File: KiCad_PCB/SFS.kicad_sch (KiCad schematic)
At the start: 28 parts, among them J4 Screw_Terminal_01x02, J6 Screw_Terminal_01x04, Q1 IRF9540N, Q2 IRLB4132, Q3 2N7000, SW1 SW_Push, SW2 SW_Push, U4 DS3231, U6 L7806

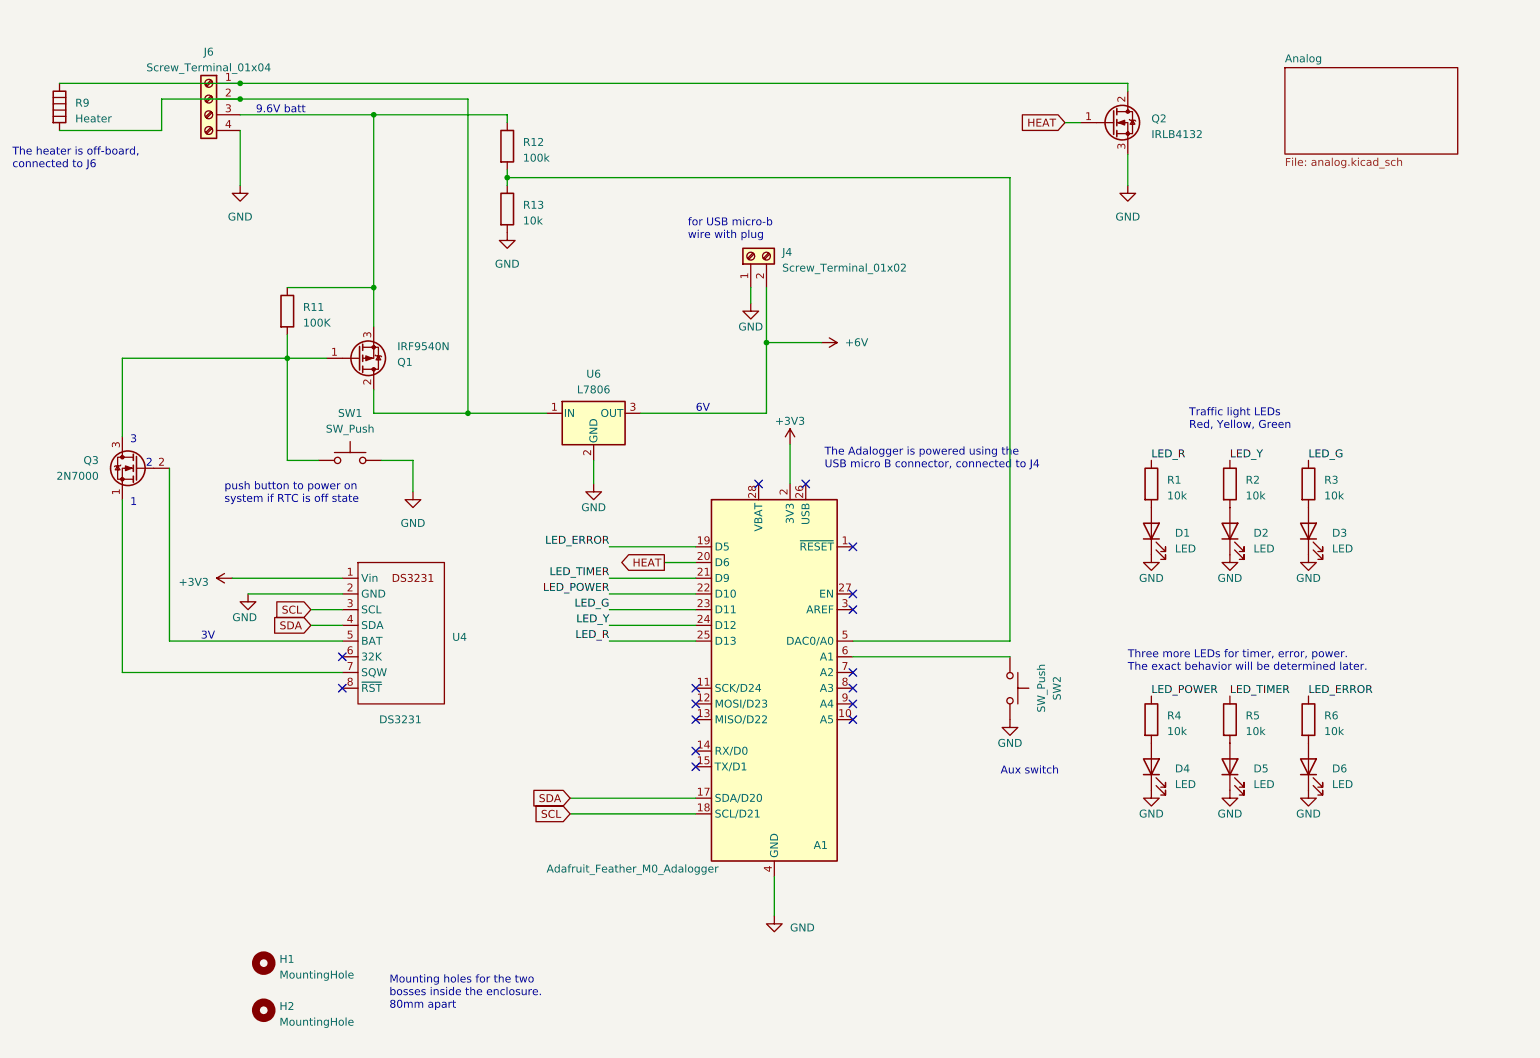
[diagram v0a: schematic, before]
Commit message: updated kicad
Updated to v2.1 from evonne's github
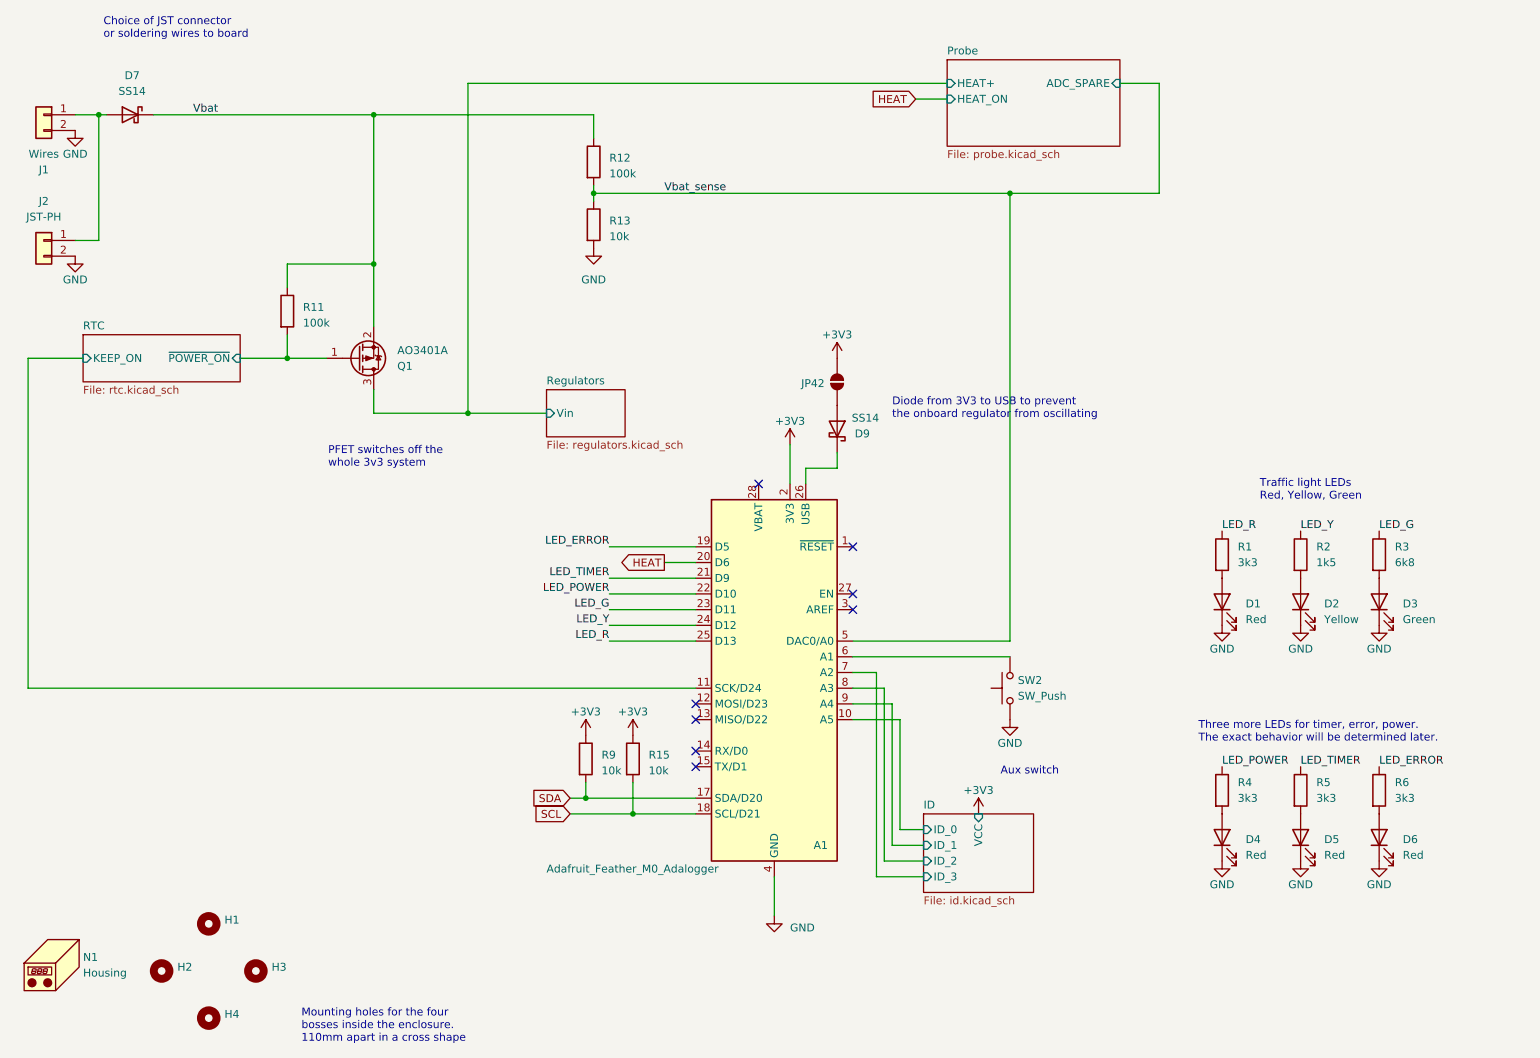
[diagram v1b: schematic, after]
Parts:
- removed J4: Screw_Terminal_01x02, SapFlow_Footprints:Wurth_Screwless45_3.81mm_2, symbol Connector:Screw_Terminal_01x02
- removed J6: Screw_Terminal_01x04, SapFlow_Footprints:Wurth_Screwless45_3.81mm_4, symbol Connector:Screw_Terminal_01x04
- removed Q1: IRF9540N, Package_TO_SOT_THT:TO-262-3_Vertical, symbol Transistor_FET:IRF9540N
- removed Q2: IRLB4132, Package_TO_SOT_THT:TO-262-3_Vertical, symbol Device:Q_NMOS_GDS
- removed Q3: 2N7000, Package_TO_SOT_THT:TO-92_Inline, symbol Transistor_FET:2N7000
- removed R9: Heater, symbol Device:Heater
- removed SW1: SW_Push, Button_Switch_THT:SW_PUSH_6mm_H4.3mm, symbol Switch:SW_Push
- removed U4: DS3231, SapFlow_Footprints:DS3231_Breakout_RightAngle, symbol New_Library:DS3231_Breakout
- removed U6: L7806, Package_TO_SOT_THT:TO-220-3_Vertical, symbol Regulator_Linear:L7806
- added D7, D9: SS14, Diode_SMD:D_SMA, symbol Diode:SS14
- added H3, H4: MountingHole, MountingHole:MountingHole_4.3mm_M4, symbol Mechanical:MountingHole
- added J1: Wires, Connector_Wire:SolderWire-0.25sqmm_1x02_P4.2mm_D0.65mm_OD1.7mm_Relief, symbol Connector_Generic:Conn_01x02
- added J2: JST-PH, Connector_JST:JST_PH_B2B-PH-K_1x02_P2.00mm_Vertical, symbol Connector_Generic:Conn_01x02
- added JP42: SolderJumper_2_Open, Jumper:SolderJumper-2_P1.3mm_Open_Pad1.0x1.5mm, symbol Jumper:SolderJumper_2_Open
- added N1: Housing, SapFlow_Footprints:Enclosure_WH-10, symbol Mechanical:Housing
- added Q1: AO3401A, Package_TO_SOT_SMD:SOT-23, symbol Transistor_FET:AO3401A
- added R15, R9: 10k, Resistor_SMD:R_0805_2012Metric_Pad1.20x1.40mm_HandSolder, symbol Device:R
- D1, D4, D5, D6: value LED -> Red; footprint LED_THT:LED_D3.0mm -> LED_SMD:LED_0603_1608Metric_Pad1.05x0.95mm_HandSolder; LCSC (none) -> C2286
- D2: value LED -> Yellow; footprint LED_THT:LED_D3.0mm -> LED_SMD:LED_0805_2012Metric_Pad1.15x1.40mm_HandSolder; LCSC (none) -> C2296
- D3: value LED -> Green; footprint LED_THT:LED_D3.0mm -> LED_SMD:LED_0805_2012Metric_Pad1.15x1.40mm_HandSolder; LCSC (none) -> C2297
- R1, R4, R5, R6: value 10k -> 3k3; footprint Resistor_THT:R_Axial_DIN0204_L3.6mm_D1.6mm_P7.62mm_Horizontal -> Resistor_SMD:R_0805_2012Metric_Pad1.20x1.40mm_HandSolder; LCSC (none) -> C26010
- R11: value 100K -> 100k; footprint Resistor_THT:R_Axial_DIN0204_L3.6mm_D1.6mm_P2.54mm_Vertical -> Resistor_SMD:R_0805_2012Metric_Pad1.20x1.40mm_HandSolder; LCSC (none) -> C149504
- R12: footprint Resistor_THT:R_Axial_DIN0204_L3.6mm_D1.6mm_P2.54mm_Vertical -> Resistor_SMD:R_0805_2012Metric_Pad1.20x1.40mm_HandSolder; LCSC (none) -> C149504
- R13: footprint Resistor_THT:R_Axial_DIN0204_L3.6mm_D1.6mm_P2.54mm_Vertical -> Resistor_SMD:R_0805_2012Metric_Pad1.20x1.40mm_HandSolder; LCSC (none) -> C17414
- R2: value 10k -> 1k5; footprint Resistor_THT:R_Axial_DIN0204_L3.6mm_D1.6mm_P7.62mm_Horizontal -> Resistor_SMD:R_0805_2012Metric_Pad1.20x1.40mm_HandSolder; LCSC (none) -> C4310
- R3: value 10k -> 6k8; footprint Resistor_THT:R_Axial_DIN0204_L3.6mm_D1.6mm_P7.62mm_Horizontal -> Resistor_SMD:R_0805_2012Metric_Pad1.20x1.40mm_HandSolder; LCSC (none) -> C17772
- SW2: footprint Button_Switch_THT:SW_PUSH_6mm_H4.3mm -> AAA_Library:SW_Push_1P1T_NO_6x6mm_H9.5mm_C2837532; LCSC (none) -> C2837532
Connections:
- net +3V3: now also JP42.2 (B), R15.1, R9.1
- net GND: now also J1.2 (Pin_2), J2.2 (Pin_2)
- net SCL: now also R15.2
- net SDA: now also R9.2
- net RTC/~{POWER_ON}: now reaches R11.2
- net RTC/~{POWER_ON}: now also Q1.1 (G)
- net Vbat_sense: now reaches A1.5 (DAC0/A0), R12.2, R13.1
- net Vbat: now reaches R11.1, R12.1
- net Vbat: now also D7.1 (K), Q1.2 (S)
- net ID/ID_0: now reaches A1.10 (A5)
- net RTC/KEEP_ON: now reaches A1.11 (SCK/D24)
- net at A1.26 (USB): now also D9.1 (K)
- net ID/ID_3: now reaches A1.7 (A2)
- net ID/ID_2: now reaches A1.8 (A3)
- net ID/ID_1: now reaches A1.9 (A4)
- new net: D7.2 (A), J1.1 (Pin_1), J2.1 (Pin_1)
- new net: D9.2 (A), JP42.1 (A)
- new net Probe/HEAT+: Q1.3 (D)
- no-connect marks 16 -> 8
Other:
- sheet Analog renamed Probe
- added sheet ID (id.kicad_sch)
- added sheet RTC (rtc.kicad_sch)
- added sheet Regulators (regulators.kicad_sch)
- sheet Probe: file analog.kicad_sch -> probe.kicad_sch
- sheet Probe ports: added ADC_SPARE, HEAT+, HEAT_ON; removed none
- note added: "Choice of JST connector or soldering wires to board"
- note added: "Diode from 3V3 to USB to prevent the onboard regulator from oscillating"
- note added: "Mounting holes for the four bosses inside the enclosure. 110mm apart in a cross shape"
- note added: "PFET switches off the whole 3v3 system"
- note removed: "1"
- note removed: "2"
- note removed: "3"
- note removed: "3V"
- note removed: "6V"
- note removed: "9.6V batt"
- note removed: "Mounting holes for the two bosses inside the enclosure. 80mm apart"
- note removed: "The Adalogger is powered using the USB micro B connector, connected to J4"
- note removed: "The heater is off-board, connected to J6"
- note removed: "for USB micro-b wire with plug"
- note removed: "push button to power on system if RTC is off state"
- moved on the sheet: D1, D2, D3, D4, D5, D6, H1, H2, R1, R12, R13, R2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
